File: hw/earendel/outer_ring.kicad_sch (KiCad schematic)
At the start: 40 parts, among them U3 IS31FL3236A-TQ

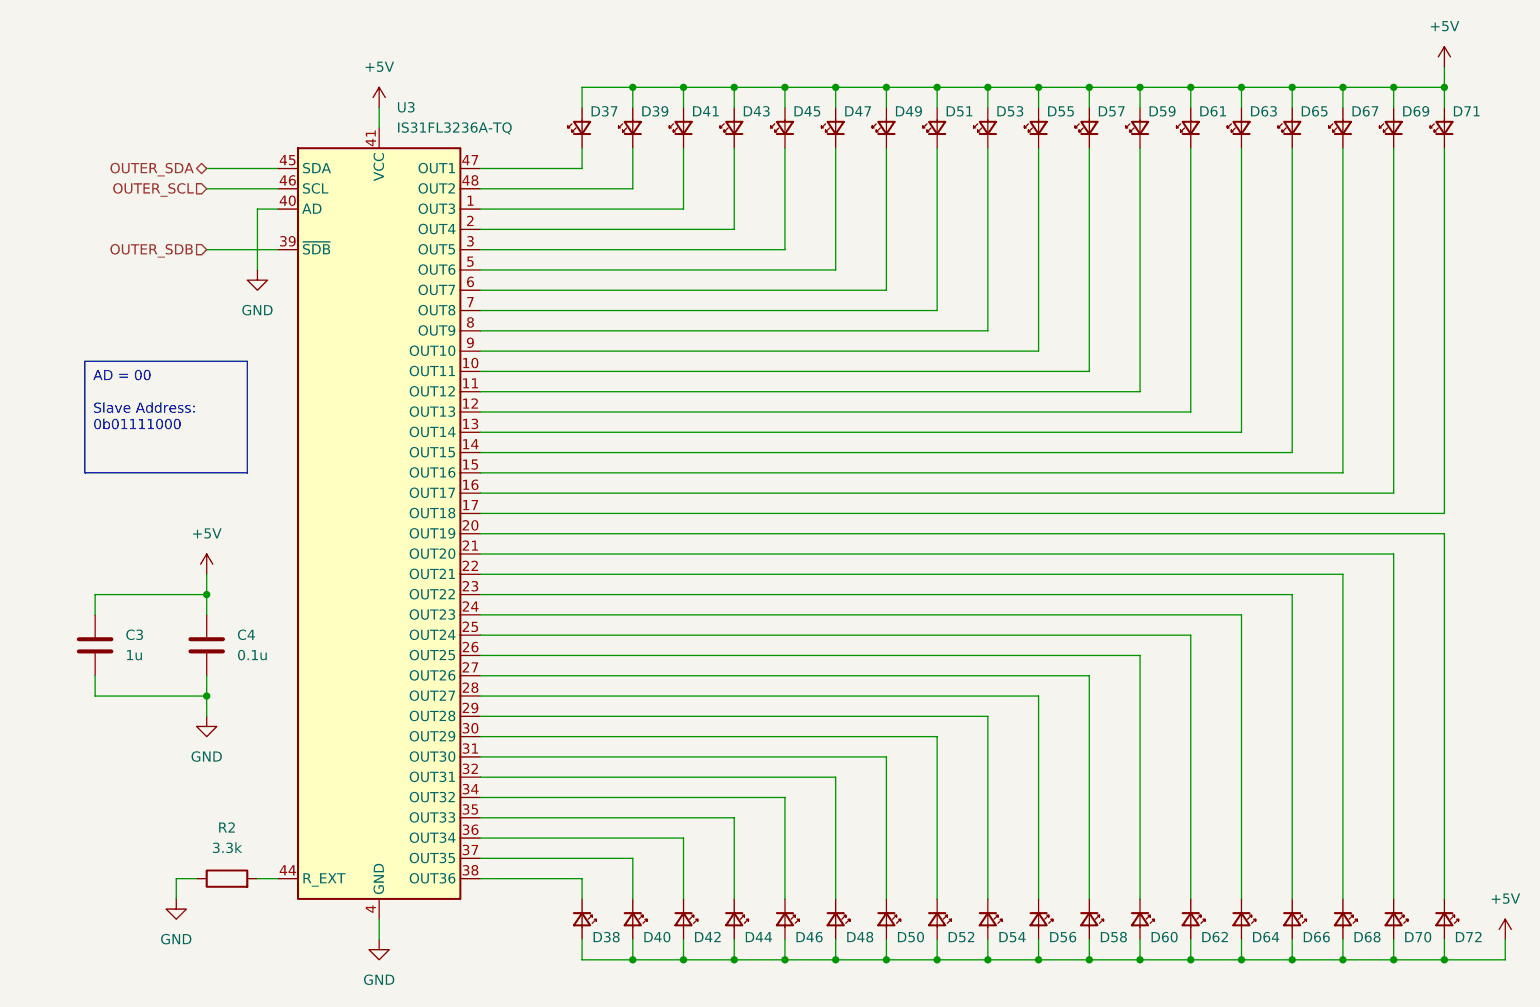
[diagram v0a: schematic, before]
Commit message: Added MCU decoupling caps, started power
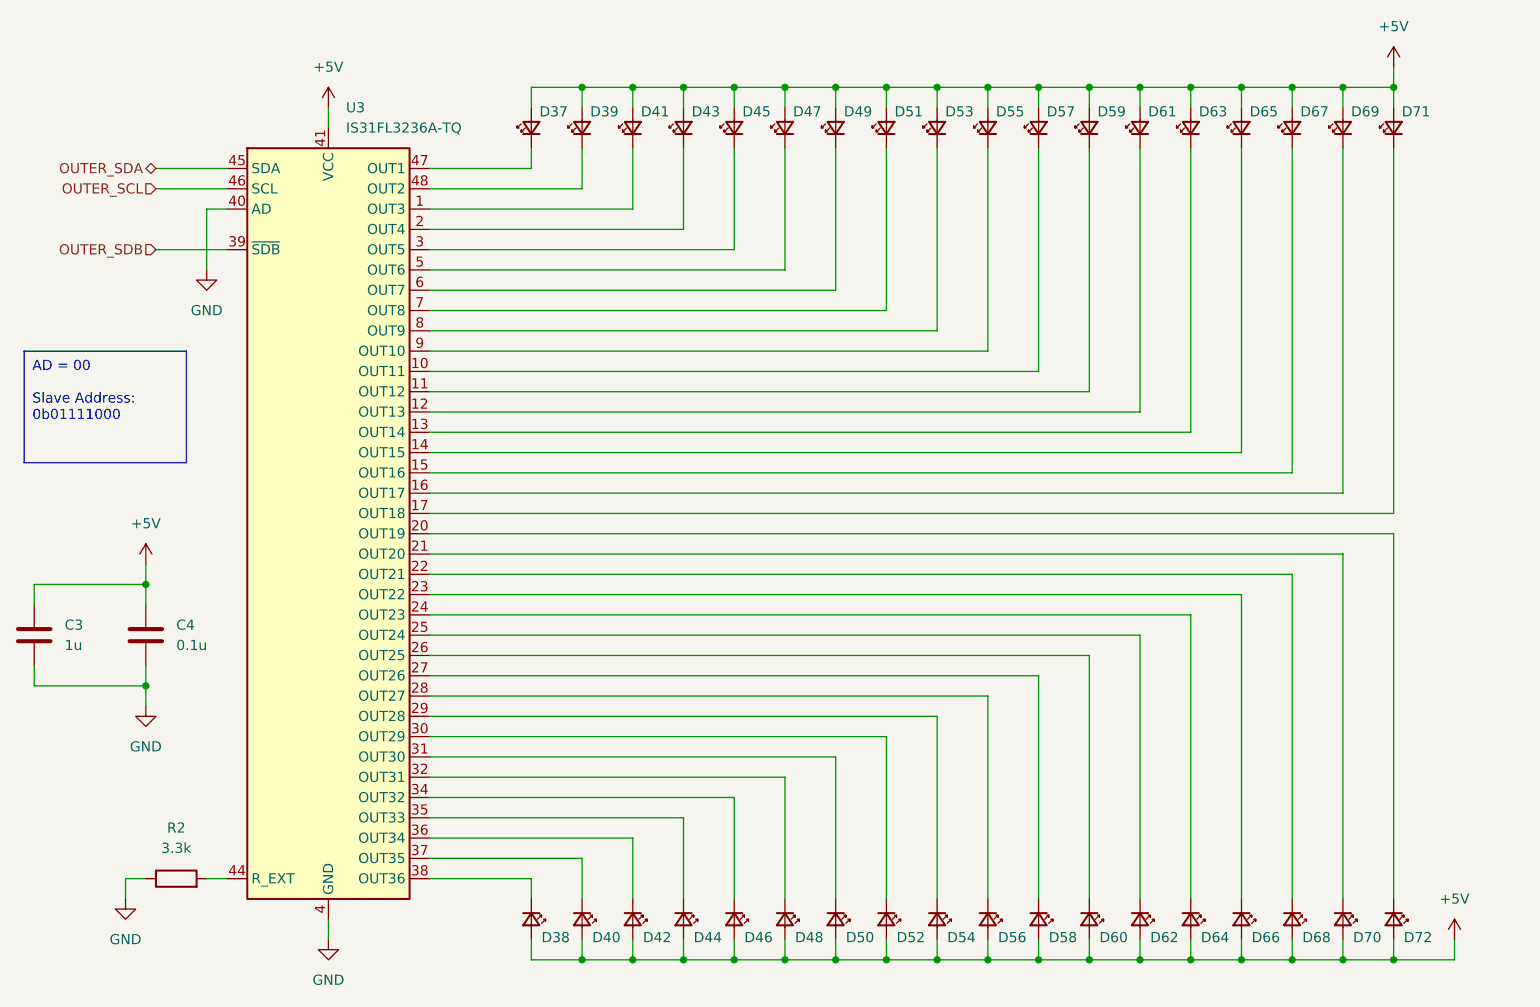
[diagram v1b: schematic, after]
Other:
- moved on the sheet: C3, C4, D37, D38, D39, D40, D41, D42, D43, D44, D45, D46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
